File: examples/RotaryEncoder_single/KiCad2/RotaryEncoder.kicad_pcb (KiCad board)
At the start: 2 copper layers, 63.5 x 33 mm, 23 parts, among them J1 Conn_01x05, SW1 Rotary Encoder Switch, U1 74HC14

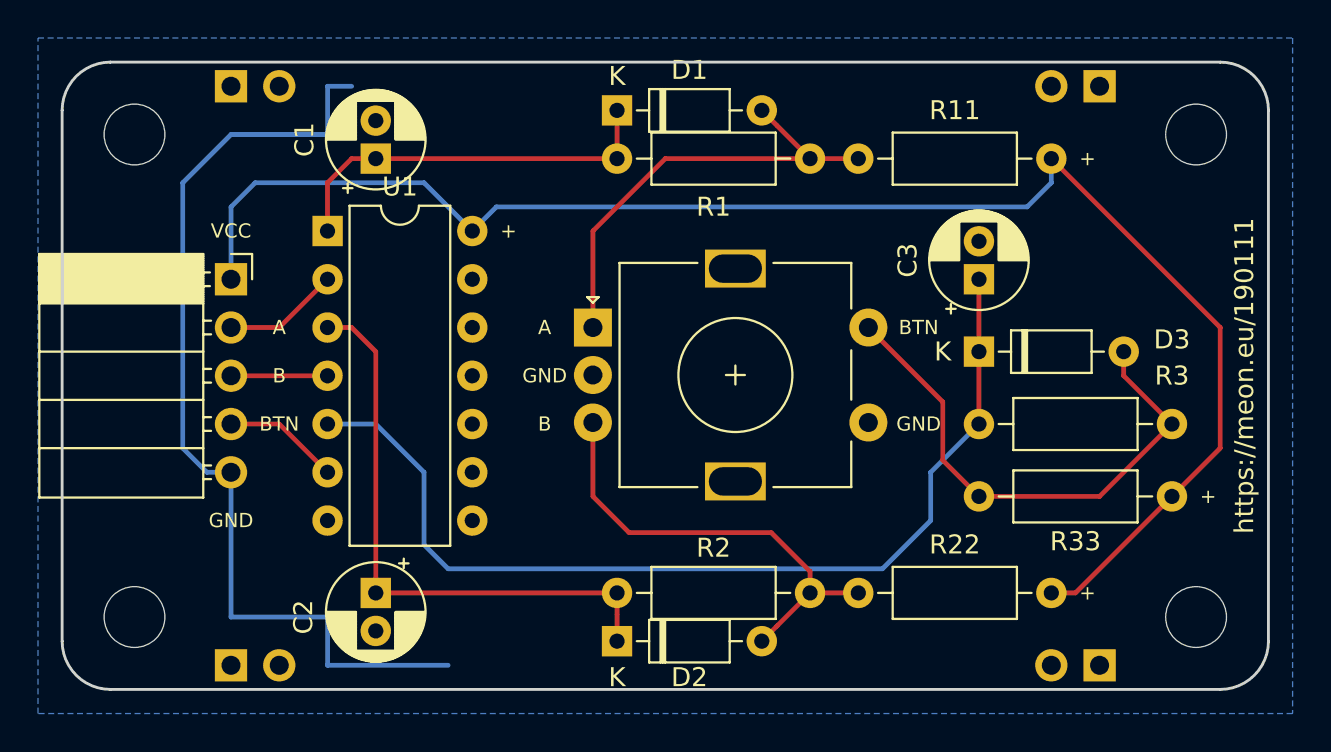
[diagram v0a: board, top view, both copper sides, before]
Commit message: use double negation to have same signals between v1 and v2
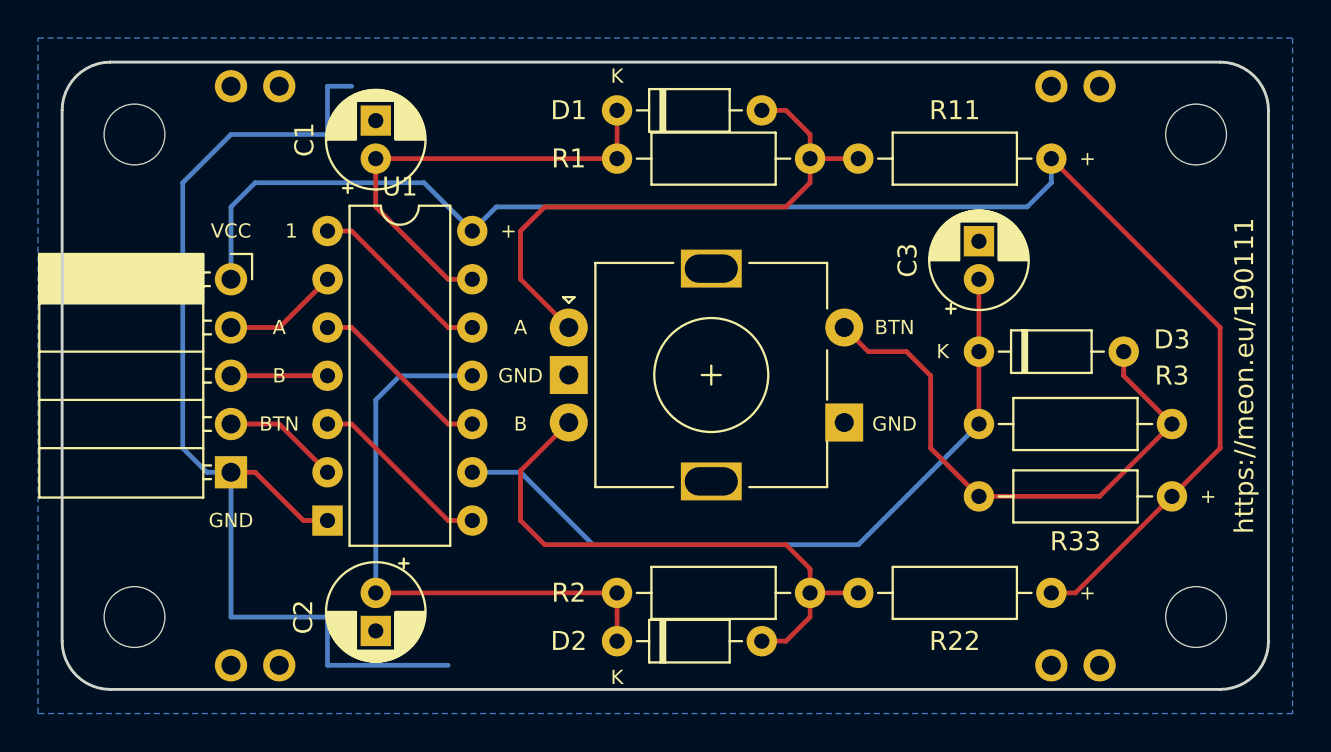
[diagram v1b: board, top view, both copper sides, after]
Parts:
- moved SW1 1.27 mm to (129.5, 78.7)
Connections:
- U1 pad 1: Net-(C1-Pad1) -> Net-(U1-Pad1)
- U1 pad 10: (no net) -> Net-(U1-Pad10)
- U1 pad 11: (no net) -> Net-(C2-Pad1)
- U1 pad 12: (no net) -> Net-(U1-Pad1)
- U1 pad 13: (no net) -> Net-(C1-Pad1)
- U1 pad 3: Net-(C2-Pad1) -> Net-(U1-Pad10)
- U1 pad 5: Net-(C3-Pad1) -> Net-(U1-Pad5)
- U1 pad 8: (no net) -> Net-(U1-Pad5)
- U1 pad 9: (no net) -> Net-(C3-Pad1)
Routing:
- net Net-(C3-Pad1): track 51.9 -> 38.5 mm
- net Net-(U1-Pad5): track 0.00 -> 9.72 mm
- net Net-(U1-Pad10): track 0.00 -> 9.72 mm
- net Net-(U1-Pad1): track 0.00 -> 9.72 mm
- net Net-(D2-Pad2): track 24.2 -> 30.7 mm
- net Net-(D1-Pad2): track 24.2 -> 30.6 mm
- net GND: track 51.1 -> 57.2 mm
- net Net-(C1-Pad1): track 20.8 -> 24.4 mm
- net Net-(D3-Pad2): track 27.9 -> 29.6 mm
- net Net-(C2-Pad1): track 32.3 -> 31.0 mm
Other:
- board text added: "1"
